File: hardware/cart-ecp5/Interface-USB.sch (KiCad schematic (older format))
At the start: 40 parts, among them J5 USB_C_USB2.0, U10 93C46BT-I_OT, U11 FT2232HQ, U3 USBLC6-2SC6, X2 DSC60xx

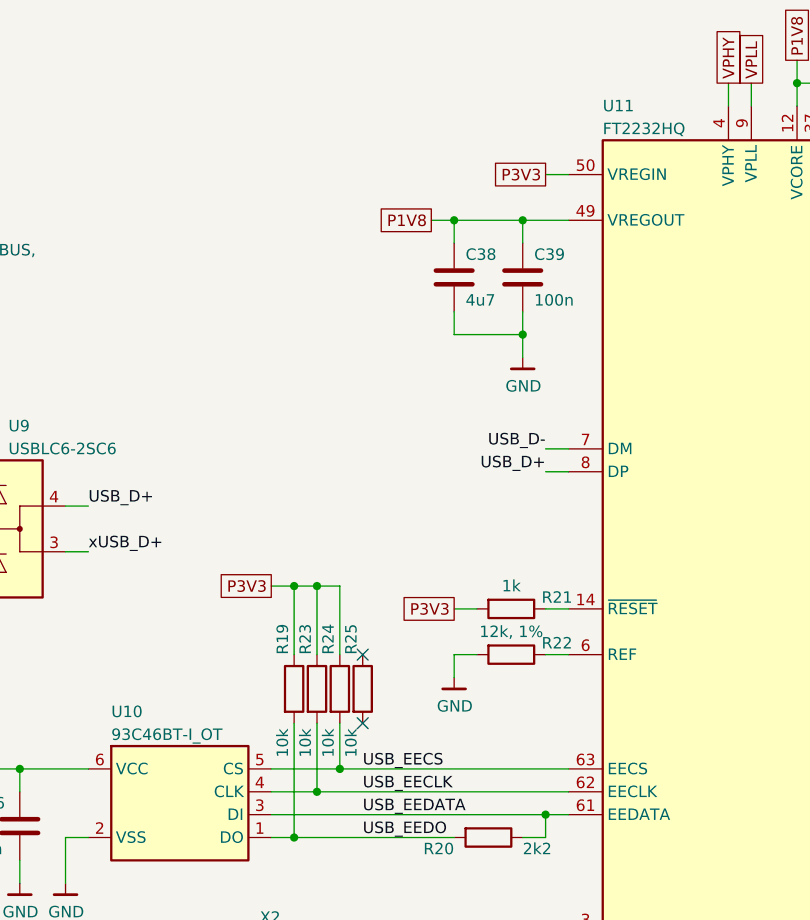
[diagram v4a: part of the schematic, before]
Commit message: Refine placement to make room for power management
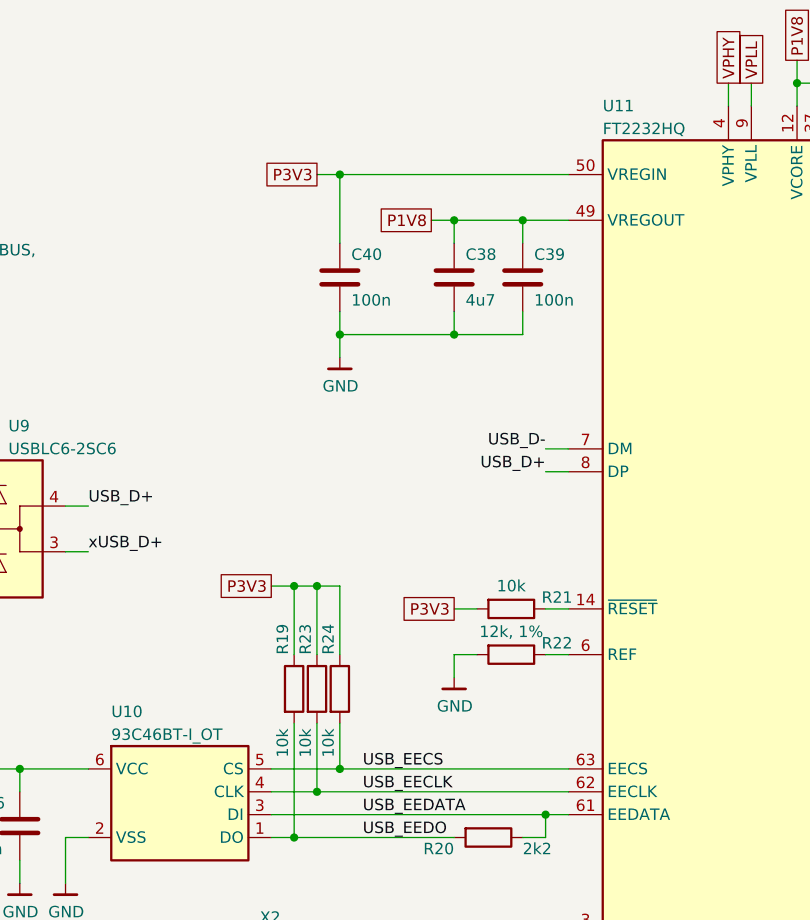
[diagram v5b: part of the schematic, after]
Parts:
- removed R25: 10k, Resistor_SMD:R_0402_1005Metric, symbol Device:R
- added C40: 100n, Capacitor_SMD:C_0402_1005Metric, symbol Device:C
- R21: value 1k -> 10k
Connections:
- net GND: now also C40.2
- net P3V3: now also C40.1
- no-connect marks 7 -> 5
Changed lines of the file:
@@
 	7450 5550 7450 5650
 Wire Wire Line
-	7550 1750 7450 1750
+	7550 1750 6550 1750
 Wire Wire Line
 	7550 1950 7350 1950
@@
 Wire Wire Line
 	6550 4350 6550 4150
-$Comp
-L Device:R R25
-U 1 1 5F1F46F9
-P 6650 4000
-F 0 "R25" V 6600 4150 50  0000 L CNN
-F 1 "10k" V 6600 3700 50  0000 L CNN
-F 2 "Resistor_SMD:R_0402_1005Metric" V 6580 4000 50  0001 C CNN
-F 3 "~" H 6650 4000 50  0001 C CNN
-F 4 "" V 6650 4000 50  0001 C CNN "MPN"
-	1    6650 4000
-	1    0    0    -1
-$EndComp
 $Comp
 L Device:R R23
@@
 	7350 2350 7350 2450
 Connection ~ 7350 1950
-Connection ~ 7350 2450
-Wire Wire Line
-	7350 2450 7350 2550
 $Comp
 L Device:C C38
@@
 Text GLabel 7050 3650 0    50   UnSpc ~ 0
 P3V3
-Text GLabel 7450 1750 0    50   UnSpc ~ 0
+Text GLabel 6450 1750 0    50   UnSpc ~ 0
 P3V3
 Text GLabel 6950 1950 0    50   UnSpc ~ 0
@@
 Text Label 6650 4650 0    50   ~ 0
 USB_EEDO
-NoConn ~ 6650 4150
-NoConn ~ 6650 3850
 $Comp
 L Device:R R19
@@
 P 7300 3650
 F 0 "R21" V 7250 3850 50  0000 C CNN
-F 1 "1k" V 7200 3650 50  0000 C CNN
+F 1 "10k" V 7200 3650 50  0000 C CNN
 F 2 "Resistor_SMD:R_0402_1005Metric" V 7230 3650 50  0001 C CNN
 F 3 "~" H 7300 3650 50  0001 C CNN
@@
 L ng_power:GND #PWR046
 U 1 1 5F7012B4
-P 7350 2550
-F 0 "#PWR046" H 7350 2300 50  0001 C CNN
-F 1 "GND" H 7353 2424 50  0000 C CNN
-F 2 "" H 7250 2200 50  0001 C CNN
-F 3 "" H 7350 2550 50  0001 C CNN
-	1    7350 2550
+P 6550 2550
+F 0 "#PWR046" H 6550 2300 50  0001 C CNN
+F 1 "GND" H 6553 2424 50  0000 C CNN
+F 2 "" H 6450 2200 50  0001 C CNN
+F 3 "" H 6550 2550 50  0001 C CNN
+	1    6550 2550
 	1    0    0    -1
 $EndComp
@@
 	9250 5950 9250 5850
 Connection ~ 9150 5950
+$Comp
+L Device:C C40
+U 1 1 5F865B3F
+P 6550 2200
+F 0 "C40" H 6500 2300 50  0000 R CNN
+F 1 "100n" H 6500 2100 50  0000 R CNN
+F 2 "Capacitor_SMD:C_0402_1005Metric" H 6588 2050 50  0001 C CNN
+F 3 "~" H 6550 2200 50  0001 C CNN
+	1    6550 2200
+	-1   0    0    -1
+$EndComp
+Wire Wire Line
+	6550 2050 6550 1750
+Connection ~ 6550 1750
+Wire Wire Line
+	6550 1750 6450 1750
+Wire Wire Line
+	6550 2350 6550 2450
+Wire Wire Line
+	6550 2450 7050 2450
+Connection ~ 7050 2450
+Wire Wire Line
+	6550 2450 6550 2550
+Connection ~ 6550 2450
 $EndSCHEMATC

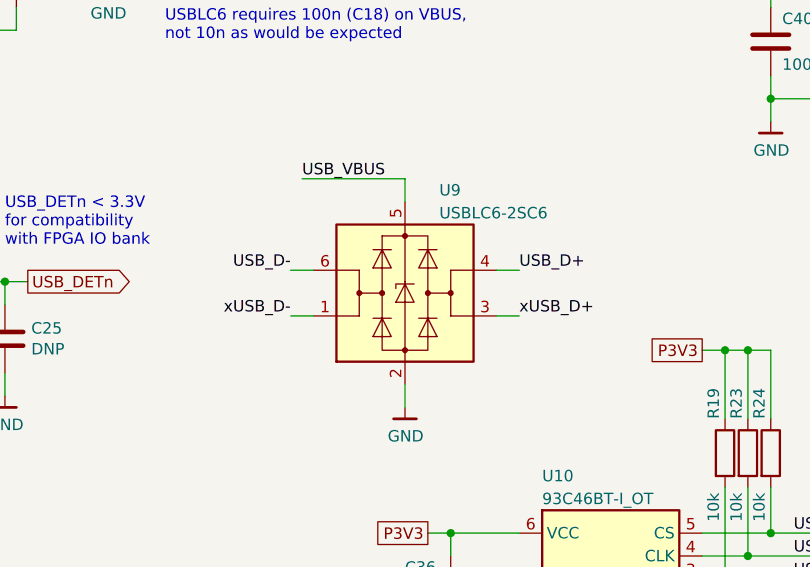
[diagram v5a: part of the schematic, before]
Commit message: Reverse USB input protection polarity
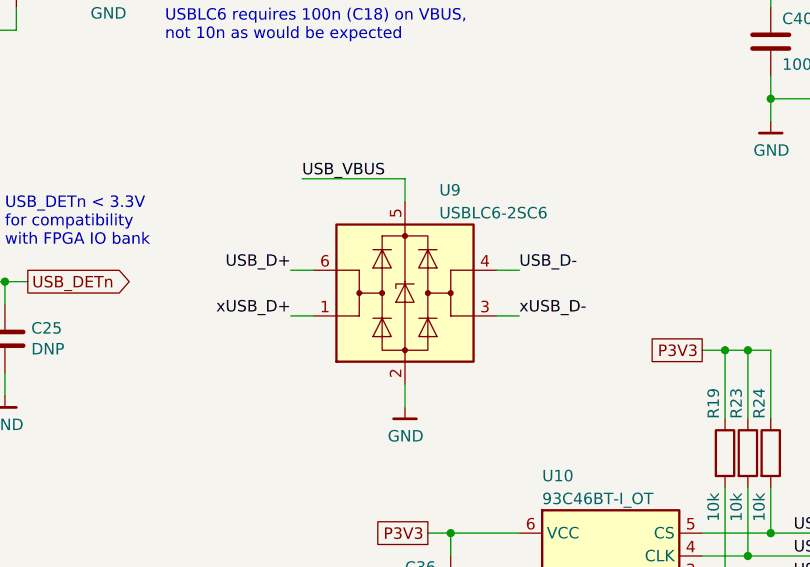
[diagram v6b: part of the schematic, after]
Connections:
- net USB_D+: now also U3.6 (I/O1); no longer U3.4 (I/O2)
- net USB_D-: now also U3.4 (I/O2); no longer U3.6 (I/O1)
- net xUSB_D+: now also U3.1 (I/O1); no longer U3.3 (I/O2)
- net xUSB_D-: now also U3.3 (I/O2); no longer U3.1 (I/O1)
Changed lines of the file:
@@
 Connection ~ 3400 6000
 Text Label 5450 3400 0    50   ~ 0
-xUSB_D+
+xUSB_D-
 Wire Wire Line
 	4550 3200 4450 3200
@@
 	5350 3200 5450 3200
 Text Label 5450 3200 0    50   ~ 0
-USB_D+
+USB_D-
 Connection ~ 4150 1850
 Wire Wire Line
@@
 +/-30ppm, <150pS
 Text Label 4450 3400 2    50   ~ 0
-xUSB_D-
+xUSB_D+
 Text Label 4450 3200 2    50   ~ 0
-USB_D-
+USB_D+
 Text Label 7450 3050 2    50   ~ 0
 USB_D+

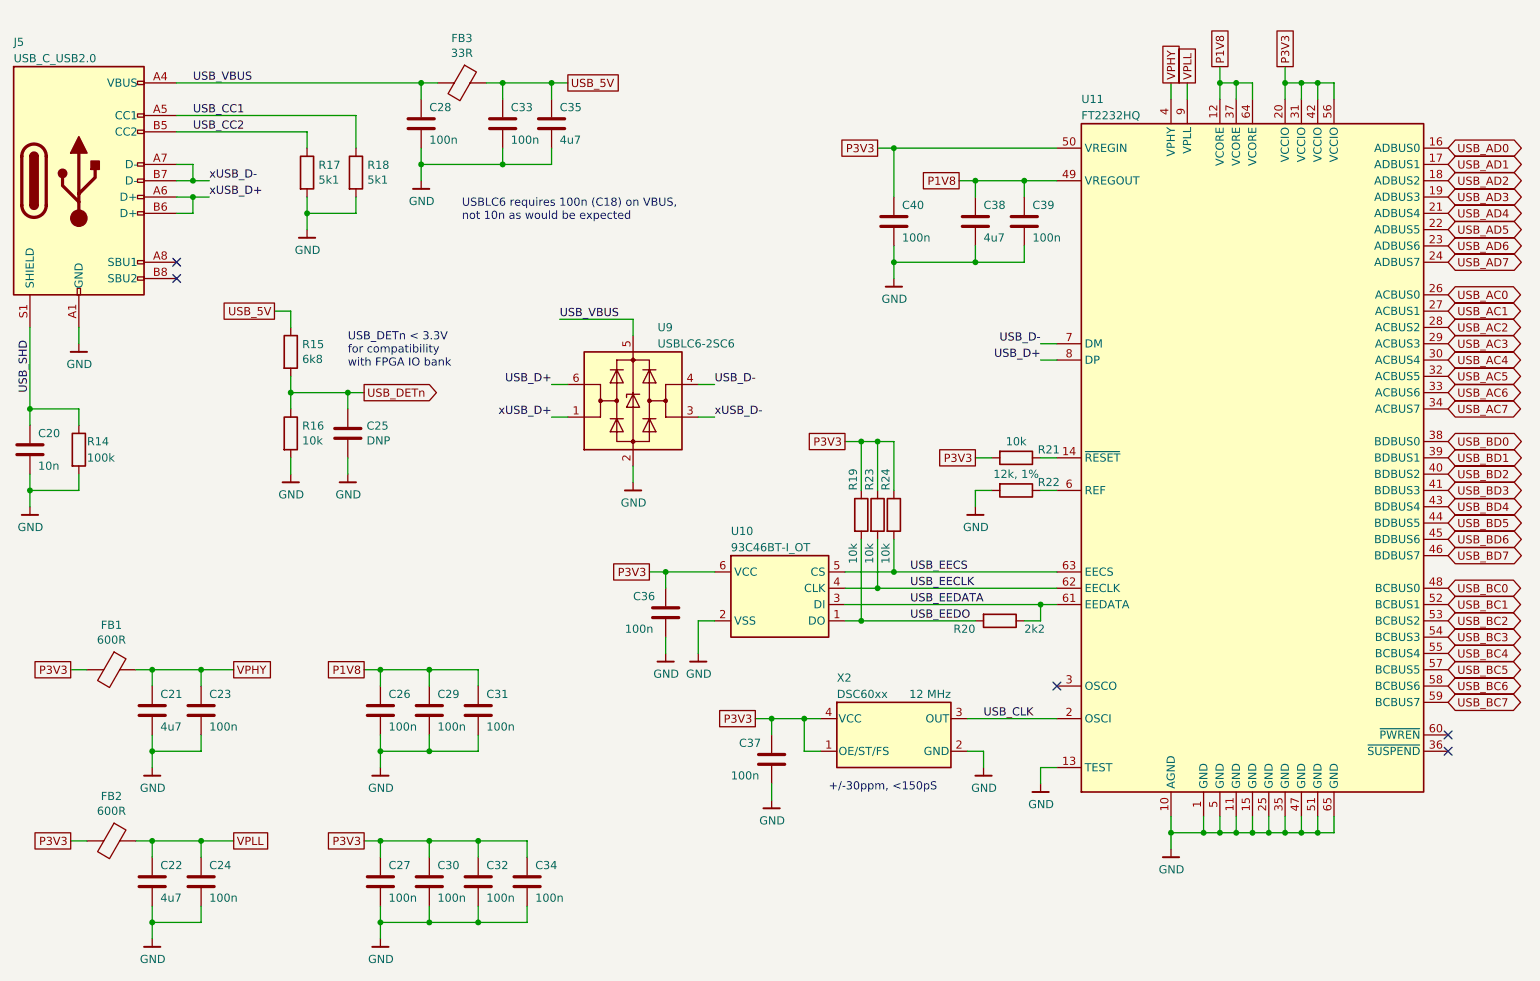
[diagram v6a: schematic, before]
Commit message: Isolate USB P1V8, VPHY, and VPLL rails to local sheet
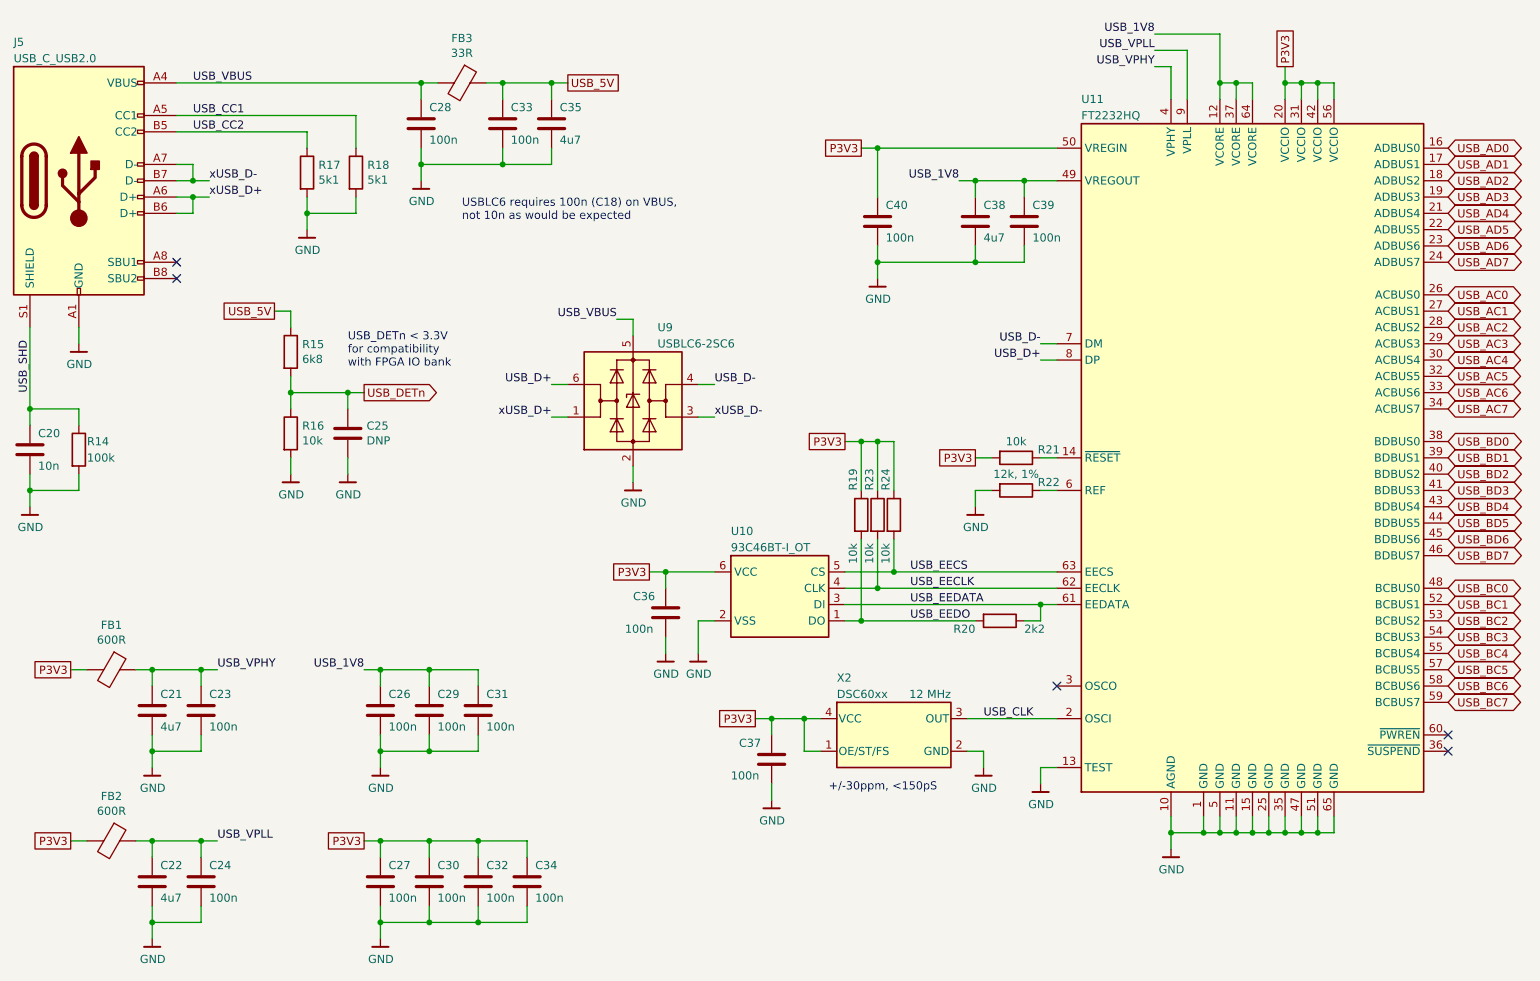
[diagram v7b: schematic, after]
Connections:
- net P1V8 renamed USB_1V8
- net VPHY renamed USB_VPHY
- net VPLL renamed USB_VPLL
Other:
- moved on the sheet: C40
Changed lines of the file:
@@
 NoConn ~ 9950 5450
 Wire Wire Line
-	8550 1350 8550 1250
+	8550 1350 8550 1050
 Connection ~ 8550 1350
 Wire Wire Line
@@
 	7450 5550 7450 5650
 Wire Wire Line
-	7550 1750 6550 1750
+	7550 1750 6450 1750
 Wire Wire Line
 	7550 1950 7350 1950
@@
 $EndComp
 Wire Wire Line
-	8250 1350 8250 1450
-Wire Wire Line
-	8350 1350 8350 1450
+	8250 1250 8250 1450
+Wire Wire Line
+	8350 1150 8350 1450
 Wire Wire Line
 	4300 6000 4300 6100
@@
 Text Notes 3900 2200 0    50   ~ 0
 USBLC6 requires 100n (C18) on VBUS,\nnot 10n as would be expected
-Text Label 4500 2800 0    50   ~ 0
+Text Label 4850 2800 2    50   ~ 0
 USB_VBUS
 $Comp
@@
 	4950 2800 4950 2900
 Wire Wire Line
-	4500 2800 4950 2800
+	4850 2800 4950 2800
 $Comp
 L Power_Protection:USBLC6-2SC6 U?
@@
 Connection ~ 2300 4950
 Wire Wire Line
-	2300 4950 2500 4950
+	2300 4950 2400 4950
 Connection ~ 2000 5450
 $Comp
@@
 	1    0    0    -1
 $EndComp
-Text GLabel 2500 4950 2    50   UnSpc ~ 0
-VPHY
 Text GLabel 1500 4950 0    50   UnSpc ~ 0
 P3V3
@@
 Connection ~ 2300 6000
 Wire Wire Line
-	2300 6000 2500 6000
+	2300 6000 2400 6000
 Connection ~ 2000 6500
 $Comp
@@
 	1    0    0    -1
 $EndComp
-Text GLabel 2500 6000 2    50   UnSpc ~ 0
-VPLL
 Text GLabel 1500 6000 0    50   UnSpc ~ 0
 P3V3
@@
 Wire Wire Line
 	3400 4950 3300 4950
-Text GLabel 3300 4950 0    50   UnSpc ~ 0
-P1V8
 Wire Wire Line
 	3400 6000 3300 6000
@@
 Text GLabel 7050 3650 0    50   UnSpc ~ 0
 P3V3
-Text GLabel 6450 1750 0    50   UnSpc ~ 0
+Text GLabel 6350 1750 0    50   UnSpc ~ 0
 P3V3
-Text GLabel 6950 1950 0    50   UnSpc ~ 0
-P1V8
 Wire Wire Line
 	6950 1950 7050 1950
 Connection ~ 7050 1950
-Text GLabel 8250 1350 1    50   UnSpc ~ 0
-VPHY
-Text GLabel 8350 1350 1    50   UnSpc ~ 0
-VPLL
-Text GLabel 8550 1250 1    50   UnSpc ~ 0
-P1V8
 Text GLabel 8950 1250 1    50   UnSpc ~ 0
 P3V3
@@
 L ng_power:GND #PWR046
 U 1 1 5F7012B4
-P 6550 2550
-F 0 "#PWR046" H 6550 2300 50  0001 C CNN
-F 1 "GND" H 6553 2424 50  0000 C CNN
-F 2 "" H 6450 2200 50  0001 C CNN
-F 3 "" H 6550 2550 50  0001 C CNN
-	1    6550 2550
+P 6450 2550
+F 0 "#PWR046" H 6450 2300 50  0001 C CNN
+F 1 "GND" H 6453 2424 50  0000 C CNN
+F 2 "" H 6350 2200 50  0001 C CNN
+F 3 "" H 6450 2550 50  0001 C CNN
+	1    6450 2550
 	1    0    0    -1
 $EndComp
@@
 L Device:C C40
 U 1 1 5F865B3F
-P 6550 2200
-F 0 "C40" H 6500 2300 50  0000 R CNN
-F 1 "100n" H 6500 2100 50  0000 R CNN
-F 2 "Capacitor_SMD:C_0402_1005Metric" H 6588 2050 50  0001 C CNN
-F 3 "~" H 6550 2200 50  0001 C CNN
-	1    6550 2200
+P 6450 2200
+F 0 "C40" H 6400 2300 50  0000 R CNN
+F 1 "100n" H 6400 2100 50  0000 R CNN
+F 2 "Capacitor_SMD:C_0402_1005Metric" H 6488 2050 50  0001 C CNN
+F 3 "~" H 6450 2200 50  0001 C CNN
+	1    6450 2200
 	-1   0    0    -1
 $EndComp
 Wire Wire Line
-	6550 2050 6550 1750
-Connection ~ 6550 1750
-Wire Wire Line
-	6550 1750 6450 1750
-Wire Wire Line
-	6550 2350 6550 2450
-Wire Wire Line
-	6550 2450 7050 2450
+	6450 2050 6450 1750
+Connection ~ 6450 1750
+Wire Wire Line
+	6450 1750 6350 1750
+Wire Wire Line
+	6450 2350 6450 2450
+Wire Wire Line
+	6450 2450 7050 2450
+Wire Wire Line
+	6450 2450 6450 2550
+Connection ~ 6450 2450
 Connection ~ 7050 2450
-Wire Wire Line
-	6550 2450 6550 2550
-Connection ~ 6550 2450
+Text Label 3300 4950 2    50   ~ 0
+USB_1V8
+Text Label 6950 1950 2    50   ~ 0
+USB_1V8
+Wire Wire Line
+	8250 1250 8150 1250
+Wire Wire Line
+	8350 1150 8150 1150
+Text Label 8150 1250 2    50   ~ 0
+USB_VPHY
+Text Label 8150 1150 2    50   ~ 0
+USB_VPLL
+Wire Wire Line
+	8550 1050 8150 1050
+Text Label 8150 1050 2    50   ~ 0
+USB_1V8
+Text Label 2400 4950 0    50   ~ 0
+USB_VPHY
+Text Label 2400 6000 0    50   ~ 0
+USB_VPLL
 $EndSCHEMATC

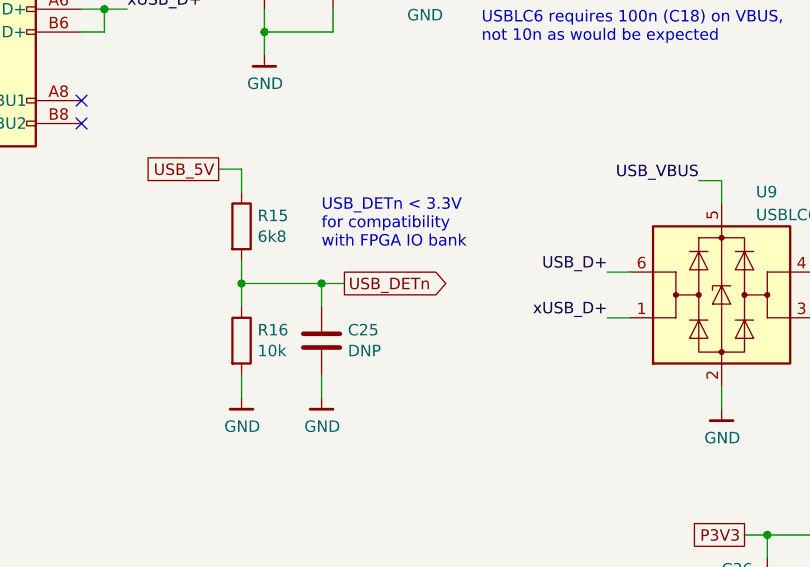
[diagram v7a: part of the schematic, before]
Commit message: Assign FPGA IO for USB_DET signal
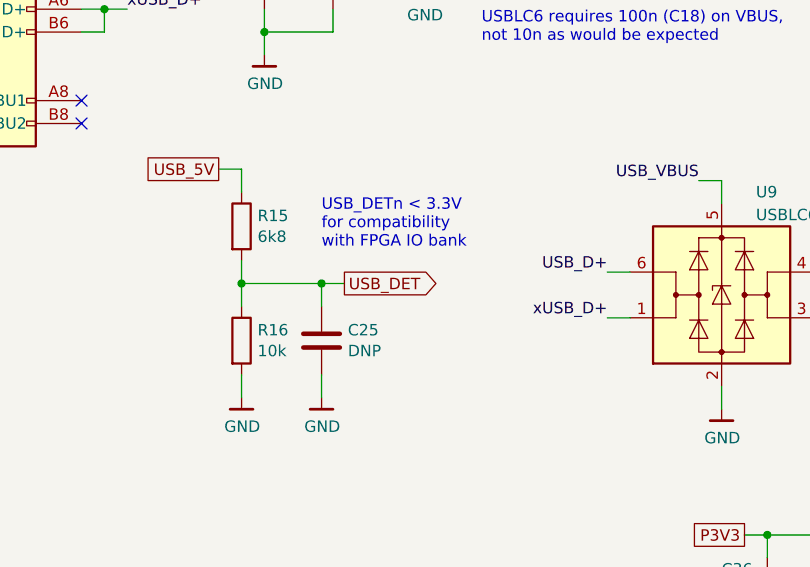
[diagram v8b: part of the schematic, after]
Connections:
- net USB_DETn renamed USB_DET
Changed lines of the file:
@@
 	2850 3250 2850 3350
 Text GLabel 3300 3250 2    50   Output ~ 0
-USB_DETn
+USB_DET
 Text GLabel 2750 2750 0    50   UnSpc ~ 0
 USB_5V
